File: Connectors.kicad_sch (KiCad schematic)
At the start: 4 parts

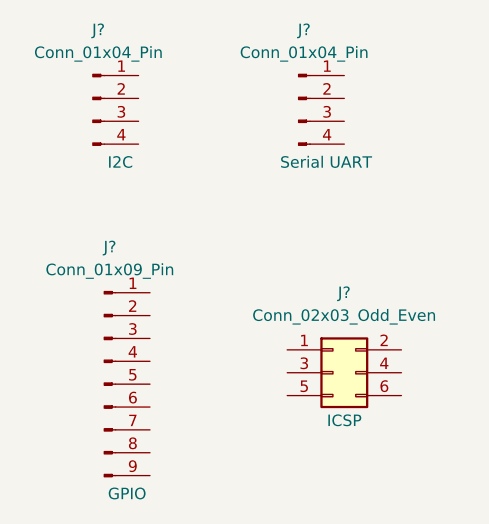
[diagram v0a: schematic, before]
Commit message: change the location of symbols(arrange) and annotate
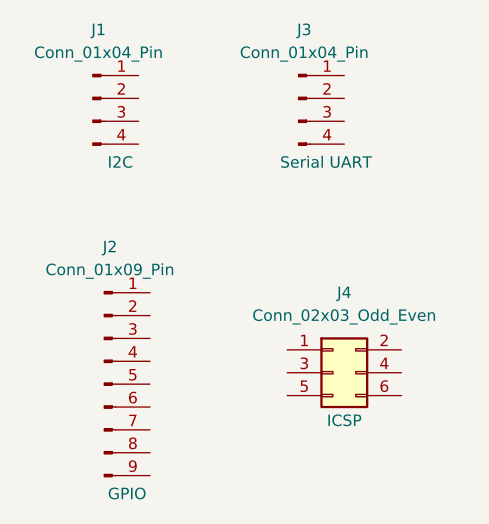
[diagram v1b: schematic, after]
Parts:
- gave numbers to parts that had none: 4
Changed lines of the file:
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@@
 		(on_board yes)
 		(dnp no)
-		(property "Reference" "J?"
+		(property "Reference" "J2"
 			(at 113.665 101.6 0)
 			(effects
@@
 			(project ""
 				(path "/d11b8ef8-3bec-4edf-bf58-e6d313bf30d2/206e5ea4-b941-4772-ae1d-8c2adfd23c6f"
-					(reference "J?")
+					(reference "J2")
 					(unit 1)
 				)
@@
 		(on_board yes)
 		(dnp no)
-		(property "Reference" "J?"
+		(property "Reference" "J4"
 			(at 139.7 106.68 0)
 			(effects
@@
 			(project ""
 				(path "/d11b8ef8-3bec-4edf-bf58-e6d313bf30d2/206e5ea4-b941-4772-ae1d-8c2adfd23c6f"
-					(reference "J?")
+					(reference "J4")
 					(unit 1)
 				)
@@
 		(on_board yes)
 		(dnp no)
-		(property "Reference" "J?"
+		(property "Reference" "J1"
 			(at 112.395 77.47 0)
 			(effects
@@
 			(project ""
 				(path "/d11b8ef8-3bec-4edf-bf58-e6d313bf30d2/206e5ea4-b941-4772-ae1d-8c2adfd23c6f"
-					(reference "J?")
+					(reference "J1")
 					(unit 1)
 				)
@@
 		(on_board yes)
 		(dnp no)
-		(property "Reference" "J?"
+		(property "Reference" "J3"
 			(at 135.255 77.47 0)
 			(effects
@@
 			(project "MCU_Datalogger"
 				(path "/d11b8ef8-3bec-4edf-bf58-e6d313bf30d2/206e5ea4-b941-4772-ae1d-8c2adfd23c6f"
-					(reference "J?")
+					(reference "J3")
 					(unit 1)
 				)

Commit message: completed symbol-footprint assignment
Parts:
- J1, J3: footprint (none) -> Connector_PinHeader_2.54mm:PinHeader_1x04_P2.54mm_Vertical
- J2: footprint (none) -> Connector_PinHeader_2.54mm:PinHeader_1x09_P2.54mm_Vertical
- J4: footprint (none) -> Connector_PinHeader_2.54mm:PinHeader_2x03_P2.54mm_Vertical
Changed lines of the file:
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@@
 			)
 		)
-		(property "Footprint" ""
+		(property "Footprint" "Connector_PinHeader_2.54mm:PinHeader_1x09_P2.54mm_Vertical"
 			(at 113.03 116.84 0)
 			(effects
@@
 			)
 		)
-		(property "Footprint" ""
+		(property "Footprint" "Connector_PinHeader_2.54mm:PinHeader_2x03_P2.54mm_Vertical"
 			(at 138.43 115.57 0)
 			(effects
@@
 			)
 		)
-		(property "Footprint" ""
+		(property "Footprint" "Connector_PinHeader_2.54mm:PinHeader_1x04_P2.54mm_Vertical"
 			(at 111.76 85.09 0)
 			(effects
@@
 			)
 		)
-		(property "Footprint" ""
+		(property "Footprint" "Connector_PinHeader_2.54mm:PinHeader_1x04_P2.54mm_Vertical"
 			(at 134.62 85.09 0)
 			(effects

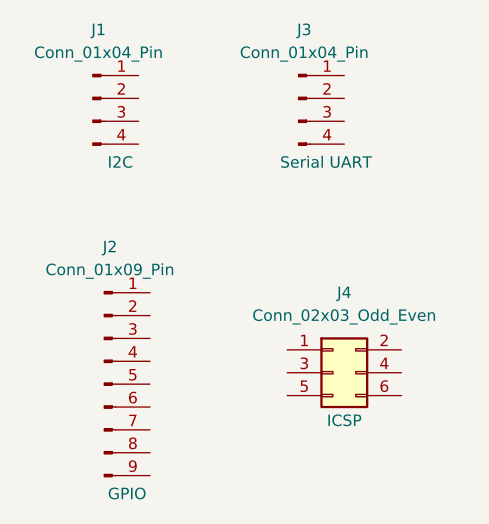
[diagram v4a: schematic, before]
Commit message: Complete wiring in second Sch
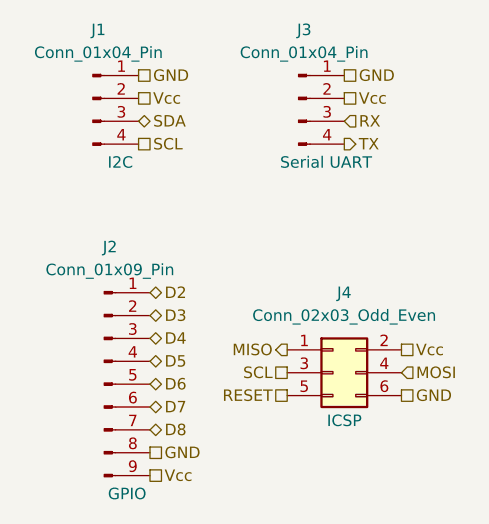
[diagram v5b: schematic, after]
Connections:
- net D2: now reaches J2.1 (Pin_1)
- net D3: now reaches J2.2 (Pin_2)
- net D4: now reaches J2.3 (Pin_3)
- net D5: now reaches J2.4 (Pin_4)
- net D6: now reaches J2.5 (Pin_5)
- net D7: now reaches J2.6 (Pin_6)
- net D8: now reaches J2.7 (Pin_7)
- net GND: now reaches J2.8 (Pin_8)
- net GND: now also J1.1 (Pin_1), J3.1 (Pin_1), J4.6 (Pin_6)
- net Vcc: now reaches J2.9 (Pin_9)
- net Vcc: now also J1.2 (Pin_2), J3.2 (Pin_2), J4.2 (Pin_2)
- net MISO: now reaches J4.1 (Pin_1)
- net SCL: now reaches J4.3 (Pin_3)
- net SCL: now also J1.4 (Pin_4)
- net MOSI: now reaches J4.4 (Pin_4)
- net RESET: now reaches J4.5 (Pin_5)
- net SDA: now reaches J1.3 (Pin_3)
- net RX: now reaches J3.3 (Pin_3)
- net TX: now reaches J3.4 (Pin_4)
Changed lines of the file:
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@@
 	(generator_version "9.0")
 	(paper "A4")
+	(hierarchical_label "SCL"
+		(shape passive)
+		(at 133.35 115.57 180)
+		(effects
+			(font
+				(size 1.27 1.27)
+			)
+			(justify right)
+		)
+	)
+	(hierarchical_label "D7"
+		(shape bidirectional)
+		(at 118.11 119.38 0)
+		(effects
+			(font
+				(size 1.27 1.27)
+			)
+			(justify left)
+		)
+	)
+	(hierarchical_label "GND"
+		(shape passive)
+		(at 116.84 82.55 0)
+		(effects
+			(font
+				(size 1.27 1.27)
+			)
+			(justify left)
+		)
+	)
+	(hierarchical_label "D2"
+		(shape bidirectional)
+		(at 118.11 106.68 0)
+		(effects
+			(font
+				(size 1.27 1.27)
+			)
+			(justify left)
+		)
+	)
+	(hierarchical_label "Vcc"
+		(shape passive)
+		(at 146.05 113.03 0)
+		(effects
+			(font
+				(size 1.27 1.27)
+			)
+			(justify left)
+		)
+	)
+	(hierarchical_label "GND"
+		(shape passive)
+		(at 139.7 82.55 0)
+		(effects
+			(font
+				(size 1.27 1.27)
+			)
+			(justify left)
+		)
+	)
+	(hierarchical_label "GND"
+		(shape passive)
+		(at 146.05 118.11 0)
+		(effects
+			(font
+				(size 1.27 1.27)
+			)
+			(justify left)
+		)
+	)
+	(hierarchical_label "GND"
+		(shape passive)
+		(at 118.11 124.46 0)
+		(effects
+			(font
+				(size 1.27 1.27)
+			)
+			(justify left)
+		)
+	)
+	(hierarchical_label "D8"
+		(shape bidirectional)
+		(at 118.11 121.92 0)
+		(effects
+			(font
+				(size 1.27 1.27)
+			)
+			(justify left)
+		)
+	)
+	(hierarchical_label "SCL"
+		(shape passive)
+		(at 116.84 90.17 0)
+		(effects
+			(font
+				(size 1.27 1.27)
+			)
+			(justify left)
+		)
+	)
+	(hierarchical_label "D3"
+		(shape bidirectional)
+		(at 118.11 109.22 0)
+		(effects
+			(font
+				(size 1.27 1.27)
+			)
+			(justify left)
+		)
+	)
+	(hierarchical_label "Vcc"
+		(shape passive)
+		(at 139.7 85.09 0)
+		(effects
+			(font
+				(size 1.27 1.27)
+			)
+			(justify left)
+		)
+	)
+	(hierarchical_label "SDA"
+		(shape bidirectional)
+		(at 116.84 87.63 0)
+		(effects
+			(font
+				(size 1.27 1.27)
+			)
+			(justify left)
+		)
+	)
+	(hierarchical_label "D6"
+		(shape bidirectional)
+		(at 118.11 116.84 0)
+		(effects
+			(font
+				(size 1.27 1.27)
+			)
+			(justify left)
+		)
+	)
+	(hierarchical_label "TX"
+		(shape output)
+		(at 139.7 90.17 0)
+		(effects
+			(font
+				(size 1.27 1.27)
+			)
+			(justify left)
+		)
+	)
+	(hierarchical_label "Vcc"
+		(shape passive)
+		(at 116.84 85.09 0)
+		(effects
+			(font
+				(size 1.27 1.27)
+			)
+			(justify left)
+		)
+	)
+	(hierarchical_label "D5"
+		(shape bidirectional)
+		(at 118.11 114.3 0)
+		(effects
+			(font
+				(size 1.27 1.27)
+			)
+			(justify left)
+		)
+	)
+	(hierarchical_label "Vcc"
+		(shape passive)
+		(at 118.11 127 0)
+		(effects
+			(font
+				(size 1.27 1.27)
+			)
+			(justify left)
+		)
+	)
+	(hierarchical_label "RESET"
+		(shape passive)
+		(at 133.35 118.11 180)
+		(effects
+			(font
+				(size 1.27 1.27)
+			)
+			(justify right)
+		)
+	)
+	(hierarchical_label "RX"
+		(shape input)
+		(at 139.7 87.63 0)
+		(effects
+			(font
+				(size 1.27 1.27)
+			)
+			(justify left)
+		)
+	)
+	(hierarchical_label "MISO"
+		(shape output)
+		(at 133.35 113.03 180)
+		(effects
+			(font
+				(size 1.27 1.27)
+			)
+			(justify right)
+		)
+	)
+	(hierarchical_label "MOSI"
+		(shape input)
+		(at 146.05 115.57 0)
+		(effects
+			(font
+				(size 1.27 1.27)
+			)
+			(justify left)
+		)
+	)
+	(hierarchical_label "D4"
+		(shape bidirectional)
+		(at 118.11 111.76 0)
+		(effects
+			(font
+				(size 1.27 1.27)
+			)
+			(justify left)
+		)
+	)
 	(symbol
 		(lib_id "Connector:Conn_01x09_Pin")
